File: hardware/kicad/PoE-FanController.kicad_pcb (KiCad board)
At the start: 2 copper layers, 56 x 78 mm, 29 parts, among them J2 FAN1, J3 FAN2, J4 FAN3, J5 FAN4, J8 Waveshare_ESP32P4POEETH, U1 LM2587-12

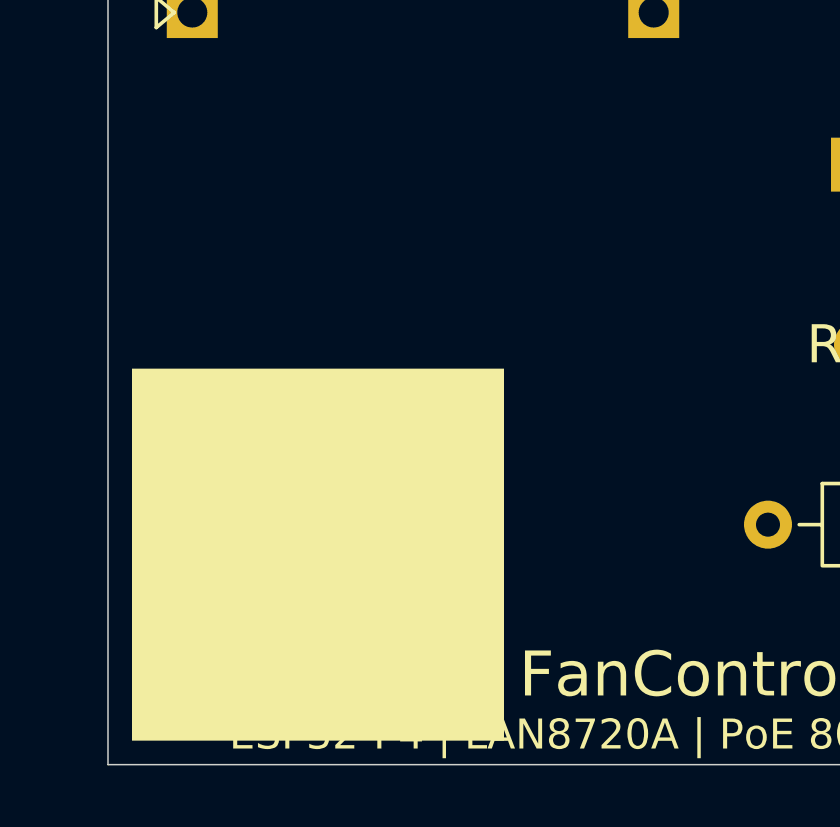
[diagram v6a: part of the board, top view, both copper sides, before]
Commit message: hw(pcb): use proper Logos footprint for NV-Home-Lab logo at (10.5, 65.5) (issue #87)
- Replace generated Custom:NV-Home-Lab-Logo polygon blob with the proper
  Logos:nv-homelab-logo-negative-15mm footprint at user-placed position (10.5, 65.5)
- Add hardware/kicad/footprints/Logos.pretty/nv-homelab-logo-negative-15mm.kicad_mod
  (migrated from hardware-self/kicad/Libraries/Logos.pretty/)
- Remove hardware-self/ directory from repo (content migrated to hardware/)
- Add hardware/generator/place_logo.py: idempotent script that checks and restores
  logo placement at (10.5, 65.5) after any PCB regeneration step
- DRC: 0 errors, 65 unconnected (expected, routing pending)

Co-authored-by: Copilot <223556219+Copilot@users.noreply.github.com>
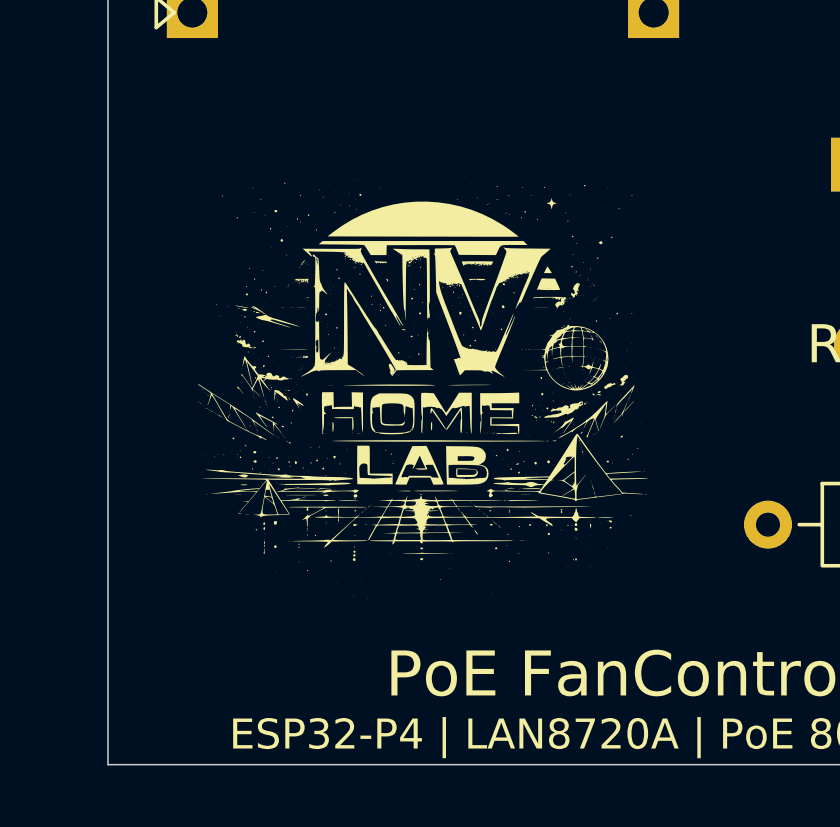
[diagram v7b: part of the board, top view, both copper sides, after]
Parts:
- removed #G1: NV-Home-Lab-Logo, Custom:NV-Home-Lab-Logo
- added G***: LOGO, Logos:nv-homelab-logo-negative-15mm, F.Cu at (10.5, 65.5)

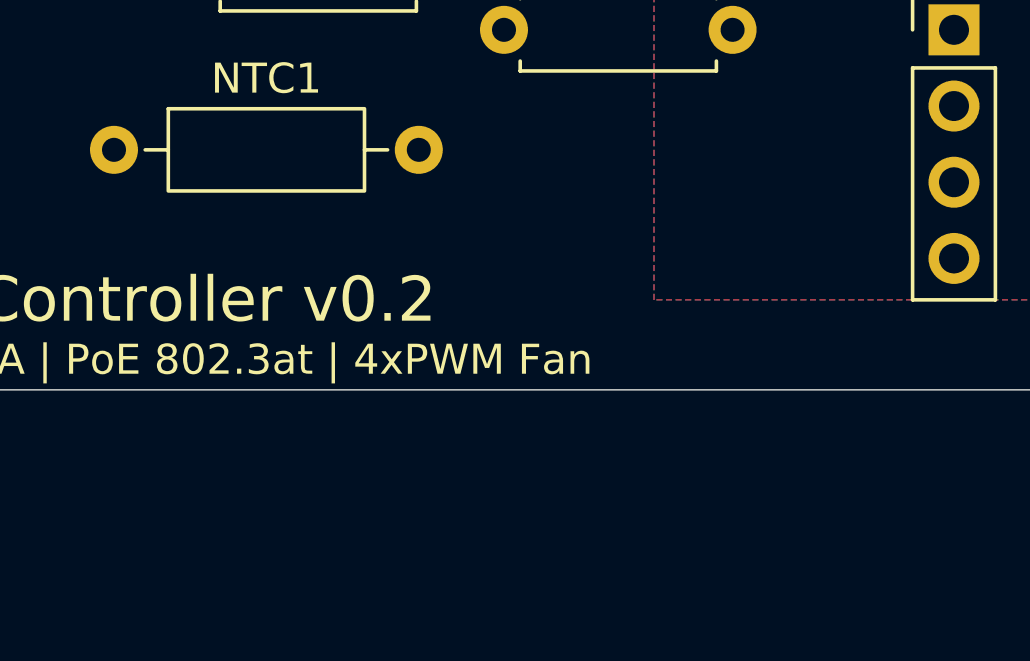
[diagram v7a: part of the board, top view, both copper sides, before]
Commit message: hw(ds18b20): place J6/R14/R15/LED6 on PCB and verify ERC/DRC
- Add hardware/add_ds18b20_pcb.py: pcbnew script that places 4 new footprints
  (J6 Molex KK-254 3-pin at 40,82; R14 4.7k at 25,82; R15 330R at 25,75;
  LED6 D3.0mm at 35,75) and assigns nets DS18B20_DATA/PROBE_LED/+3V3/GND
- Add 2 routing traces: PROBE_LED_A (R15 pin2->LED6 pin1) and DS18B20_DATA
  local U-route from R14 pin2 to J6 pin2
- Update import_netlist.py: add J8 pins 27/28 and new component pad net assignments
- Update firmware/include/pins.h: add DS18B20_DATA_PIN=19 and PROBE_LED_PIN=20
- Regenerate netlist (netlist.kicad_net) with DS18B20_DATA/PROBE_LED nets
- ERC: 0 errors, 83 warnings (all pre-existing lib_symbol_mismatch/warnings)
- DRC: exit code 0; 28 warnings (all pre-existing types); 71 unconnected
  (65 pre-existing + 6 new, consistent with ROUTING_PENDING project state)
- Mark T001-T018 complete in tasks.md (T006 partial: J8 long traces and
  power-pour connections deferred to KiCad GUI per ROUTING_PENDING convention)
- Native tests: 22/22 passing (test_probe 5/5, test_pins 10/10,
  test_fan 3/3, test_ota 4/4) with MinGW in PATH

Refs #97
Task: T003 T004 T005 T006 T007 T009
Issue: #97

Co-authored-by: Copilot <223556219+Copilot@users.noreply.github.com>
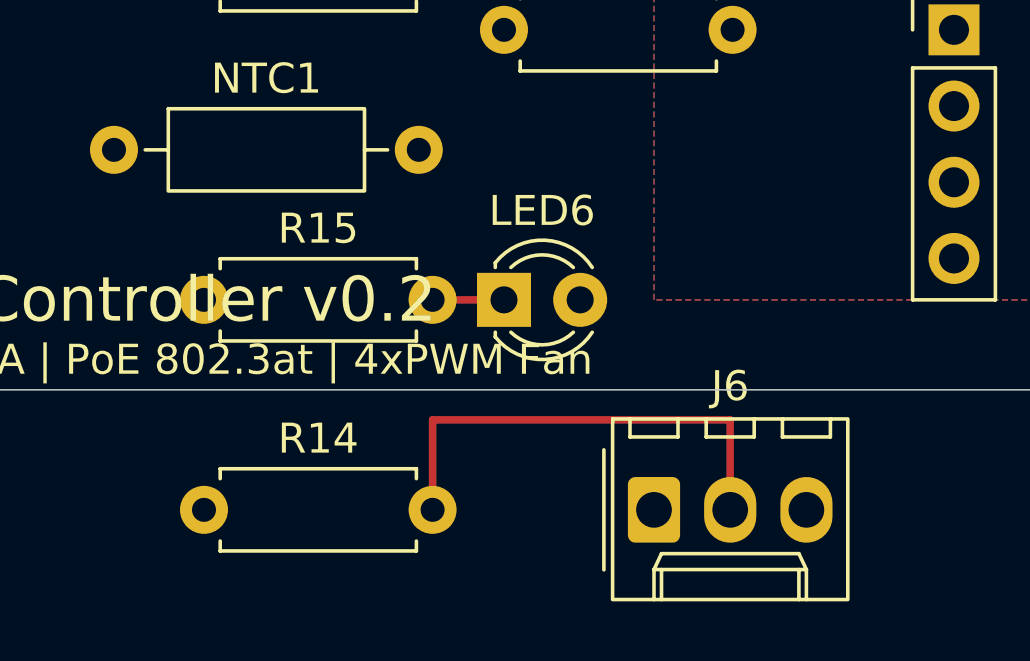
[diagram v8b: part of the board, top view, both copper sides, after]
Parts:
- added J6: Molex_KK254_3pin, Molex_KK-254_AE-6410-03A_1x03_P2.54mm_Vertical, F.Cu at (40.0, 82.0)
- added LED6: LED_GREEN, LED_D3.0mm, F.Cu at (35.0, 75.0)
- added R14: 4k7, R_Axial_DIN0207_L6.3mm_D2.5mm_P7.62mm_Horizontal, F.Cu at (25.0, 82.0)
- added R15: 330R, R_Axial_DIN0207_L6.3mm_D2.5mm_P7.62mm_Horizontal, F.Cu at (25.0, 75.0)
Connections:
- J8 pad 27: unconnected-(J8-NC-Pad27) -> DS18B20_DATA
- J8 pad 28: unconnected-(J8-NC-Pad28) -> PROBE_LED
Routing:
- net DS18B20_DATA: track 0.00 -> 15.9 mm
- net /PROBE_LED_A: track 0.00 -> 2.38 mm
